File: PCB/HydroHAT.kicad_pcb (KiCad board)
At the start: 2 copper layers, 65 x 56 mm, 0 parts

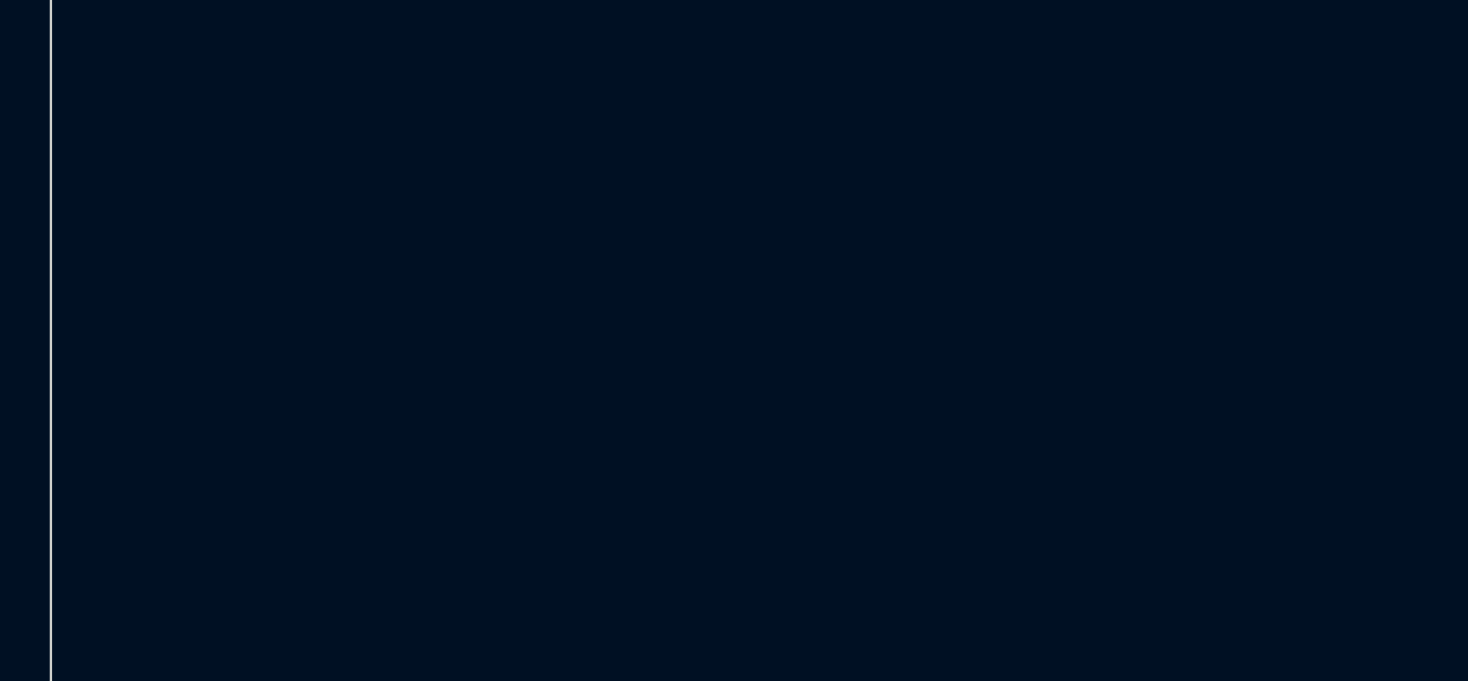
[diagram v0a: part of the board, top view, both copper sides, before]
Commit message: Schematic start
And mostly done, still need to add FTDI
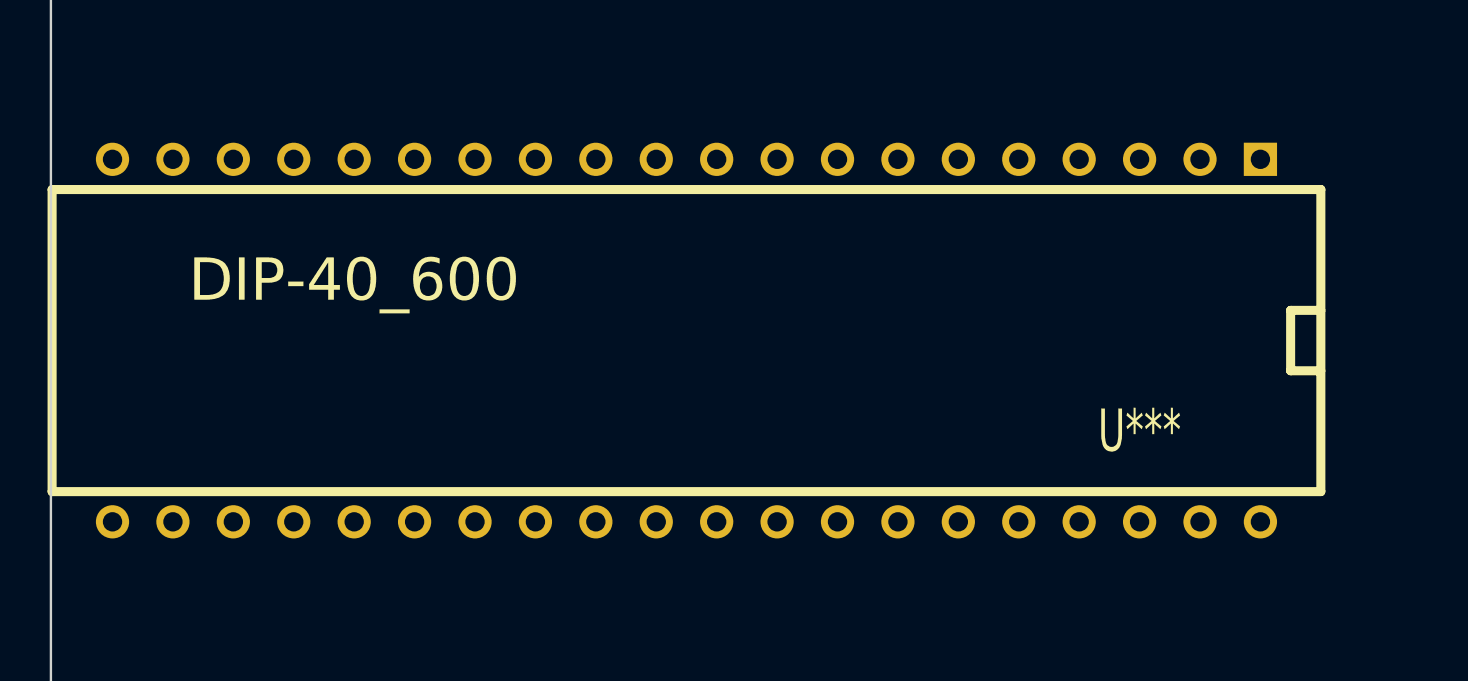
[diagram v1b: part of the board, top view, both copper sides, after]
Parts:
- added U***: DIP-40_600, DIP-40__600, F.Cu at (45.7, 47.0)
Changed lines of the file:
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@@
     (links 0)
     (no_connects 0)
-    (area 0 0 0 0)
+    (area 18.949999 18.949999 84.050001 75.050001)
     (thickness 1.6)
     (drawings 8)
     (tracks 0)
     (zones 0)
-    (modules 0)
+    (modules 1)
     (nets 1)
   )
@@
     (pad_to_mask_clearance 0)
     (aux_axis_origin 0 0)
-    (visible_elements FFFFFFBF)
+    (visible_elements 7FFFFFFF)
     (pcbplotparams
       (layerselection 3178497)
@@
     (add_net "")
   )
+  (module DIP-40__600 (layer F.Cu)
+    (at 45.72 46.99 180)
+    (descr "Module Dil 40 pins, pads ronds, e=600 mils")
+    (tags DIL)
+    (fp_text reference U*** (at -19.05 -3.81 180) (layer F.SilkS)
+      (effects (font (size 1.778 1.143) (thickness 0.3048)))
+    )
+    (fp_text value DIP-40_600 (at 13.97 2.54 180) (layer F.SilkS)
+      (effects (font (size 1.778 1.778) (thickness 0.3048)))
+    )
+    (fp_line (start -26.67 -1.27) (end -25.4 -1.27) (layer F.SilkS) (width 0.381))
+    (fp_line (start -25.4 -1.27) (end -25.4 1.27) (layer F.SilkS) (width 0.381))
+    (fp_line (start -25.4 1.27) (end -26.67 1.27) (layer F.SilkS) (width 0.381))
+    (fp_line (start -26.67 -6.35) (end 26.67 -6.35) (layer F.SilkS) (width 0.381))
+    (fp_line (start 26.67 -6.35) (end 26.67 6.35) (layer F.SilkS) (width 0.381))
+    (fp_line (start 26.67 6.35) (end -26.67 6.35) (layer F.SilkS) (width 0.381))
+    (fp_line (start -26.67 6.35) (end -26.67 -6.35) (layer F.SilkS) (width 0.381))
+    (pad 1 thru_hole rect (at -24.13 7.62 180) (size 1.397 1.397) (drill 0.8128)
+      (layers *.Cu *.Mask F.SilkS)
+    )
+    (pad 2 thru_hole circle (at -21.59 7.62 180) (size 1.397 1.397) (drill 0.8128)
+      (layers *.Cu *.Mask F.SilkS)
+    )
+    (pad 3 thru_hole circle (at -19.05 7.62 180) (size 1.397 1.397) (drill 0.8128)
+      (layers *.Cu *.Mask F.SilkS)
+    )
+    (pad 4 thru_hole circle (at -16.51 7.62 180) (size 1.397 1.397) (drill 0.8128)
+      (layers *.Cu *.Mask F.SilkS)
+    )
+    (pad 5 thru_hole circle (at -13.97 7.62 180) (size 1.397 1.397) (drill 0.8128)
+      (layers *.Cu *.Mask F.SilkS)
+    )
+    (pad 6 thru_hole circle (at -11.43 7.62 180) (size 1.397 1.397) (drill 0.8128)
+      (layers *.Cu *.Mask F.SilkS)
+    )
+    (pad 7 thru_hole circle (at -8.89 7.62 180) (size 1.397 1.397) (drill 0.8128)
+      (layers *.Cu *.Mask F.SilkS)
+    )
+    (pad 8 thru_hole circle (at -6.35 7.62 180) (size 1.397 1.397) (drill 0.8128)
+      (layers *.Cu *.Mask F.SilkS)
+    )
+    (pad 9 thru_hole circle (at -3.81 7.62 180) (size 1.397 1.397) (drill 0.8128)
+      (layers *.Cu *.Mask F.SilkS)
+    )
+    (pad 10 thru_hole circle (at -1.27 7.62 180) (size 1.397 1.397) (drill 0.8128)
+      (layers *.Cu *.Mask F.SilkS)
+    )
+    (pad 11 thru_hole circle (at 1.27 7.62 180) (size 1.397 1.397) (drill 0.8128)
+      (layers *.Cu *.Mask F.SilkS)
+    )
+    (pad 12 thru_hole circle (at 3.81 7.62 180) (size 1.397 1.397) (drill 0.8128)
+      (layers *.Cu *.Mask F.SilkS)
+    )
+    (pad 13 thru_hole circle (at 6.35 7.62 180) (size 1.397 1.397) (drill 0.8128)
+      (layers *.Cu *.Mask F.SilkS)
+    )
+    (pad 14 thru_hole circle (at 8.89 7.62 180) (size 1.397 1.397) (drill 0.8128)
+      (layers *.Cu *.Mask F.SilkS)
+    )
+    (pad 15 thru_hole circle (at 11.43 7.62 180) (size 1.397 1.397) (drill 0.8128)
+      (layers *.Cu *.Mask F.SilkS)
+    )
+    (pad 16 thru_hole circle (at 13.97 7.62 180) (size 1.397 1.397) (drill 0.8128)
+      (layers *.Cu *.Mask F.SilkS)
+    )
+    (pad 17 thru_hole circle (at 16.51 7.62 180) (size 1.397 1.397) (drill 0.8128)
+      (layers *.Cu *.Mask F.SilkS)
+    )
+    (pad 18 thru_hole circle (at 19.05 7.62 180) (size 1.397 1.397) (drill 0.8128)
+      (layers *.Cu *.Mask F.SilkS)
+    )
+    (pad 19 thru_hole circle (at 21.59 7.62 180) (size 1.397 1.397) (drill 0.8128)
+      (layers *.Cu *.Mask F.SilkS)
+    )
+    (pad 20 thru_hole circle (at 24.13 7.62 180) (size 1.397 1.397) (drill 0.8128)
+      (layers *.Cu *.Mask F.SilkS)
+    )
+    (pad 21 thru_hole circle (at 24.13 -7.62 180) (size 1.397 1.397) (drill 0.8128)
+      (layers *.Cu *.Mask F.SilkS)
+    )
+    (pad 22 thru_hole circle (at 21.59 -7.62 180) (size 1.397 1.397) (drill 0.8128)
+      (layers *.Cu *.Mask F.SilkS)
+    )
+    (pad 23 thru_hole circle (at 19.05 -7.62 180) (size 1.397 1.397) (drill 0.8128)
+      (layers *.Cu *.Mask F.SilkS)
+    )
+    (pad 24 thru_hole circle (at 16.51 -7.62 180) (size 1.397 1.397) (drill 0.8128)
+      (layers *.Cu *.Mask F.SilkS)
+    )
+    (pad 25 thru_hole circle (at 13.97 -7.62 180) (size 1.397 1.397) (drill 0.8128)
+      (layers *.Cu *.Mask F.SilkS)
+    )
+    (pad 26 thru_hole circle (at 11.43 -7.62 180) (size 1.397 1.397) (drill 0.8128)
+      (layers *.Cu *.Mask F.SilkS)
+    )
+    (pad 27 thru_hole circle (at 8.89 -7.62 180) (size 1.397 1.397) (drill 0.8128)
+      (layers *.Cu *.Mask F.SilkS)
+    )
+    (pad 28 thru_hole circle (at 6.35 -7.62 180) (size 1.397 1.397) (drill 0.8128)
+      (layers *.Cu *.Mask F.SilkS)
+    )
+    (pad 29 thru_hole circle (at 3.81 -7.62 180) (size 1.397 1.397) (drill 0.8128)
+      (layers *.Cu *.Mask F.SilkS)
+    )
+    (pad 30 thru_hole circle (at 1.27 -7.62 180) (size 1.397 1.397) (drill 0.8128)
+      (layers *.Cu *.Mask F.SilkS)
+    )
+    (pad 31 thru_hole circle (at -1.27 -7.62 180) (size 1.397 1.397) (drill 0.8128)
+      (layers *.Cu *.Mask F.SilkS)
+    )
+    (pad 32 thru_hole circle (at -3.81 -7.62 180) (size 1.397 1.397) (drill 0.8128)
+      (layers *.Cu *.Mask F.SilkS)
+    )
+    (pad 33 thru_hole circle (at -6.35 -7.62 180) (size 1.397 1.397) (drill 0.8128)
+      (layers *.Cu *.Mask F.SilkS)
+    )
+    (pad 34 thru_hole circle (at -8.89 -7.62 180) (size 1.397 1.397) (drill 0.8128)
+      (layers *.Cu *.Mask F.SilkS)
+    )
+    (pad 35 thru_hole circle (at -11.43 -7.62 180) (size 1.397 1.397) (drill 0.8128)
+      (layers *.Cu *.Mask F.SilkS)
+    )
+    (pad 36 thru_hole circle (at -13.97 -7.62 180) (size 1.397 1.397) (drill 0.8128)
+      (layers *.Cu *.Mask F.SilkS)
+    )
+    (pad 37 thru_hole circle (at -16.51 -7.62 180) (size 1.397 1.397) (drill 0.8128)
+      (layers *.Cu *.Mask F.SilkS)
+    )
+    (pad 38 thru_hole circle (at -19.05 -7.62 180) (size 1.397 1.397) (drill 0.8128)
+      (layers *.Cu *.Mask F.SilkS)
+    )
+    (pad 39 thru_hole circle (at -21.59 -7.62 180) (size 1.397 1.397) (drill 0.8128)
+      (layers *.Cu *.Mask F.SilkS)
+    )
+    (pad 40 thru_hole circle (at -24.13 -7.62 180) (size 1.397 1.397) (drill 0.8128)
+      (layers *.Cu *.Mask F.SilkS)
+    )
+    (model dil/dil_40-w600.wrl
+      (at (xyz 0 0 0))
+      (scale (xyz 1 1 1))
+      (rotate (xyz 0 0 0))
+    )
+  )
   (gr_line (start 81 19) (end 22 19) (angle 90) (layer Edge.Cuts) (width 0.1))
